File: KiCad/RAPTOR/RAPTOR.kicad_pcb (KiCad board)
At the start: 2 copper layers, 101.6 x 101.6 mm, 29 parts, among them J1 SOLC_CONN, J10 EXT_LED3, J11 SRVOL_CONN, J12 SRVOR_CONN, J14 RBF_CONN, J15 EEP_BTN_CONN, J18 CONN_BUZZER, J2 SOLP_CONN, J3 JST_2MM_MALE, J4 CONN_LED_FIX, J5 EXTENSION_HEADER, J7 EXT_LED0, J8 EXT_LED1, J9 EXT_LED2, Q1 MOSFET-NCH-STQ2NK60ZR-AP, Q2 MOSFET-NCH-STQ2NK60ZR-AP, Q3 MOSFET-NCH-STQ2NK60ZR-AP, Q4 MOSFET-NCH-STQ2NK60ZR-AP, U1 BMP280 Breakout, U2 BNO055 Breakout, U3 OpenLog, U4 AdafruitGPS, U5 Teensy3.2, U6 D24V550F5

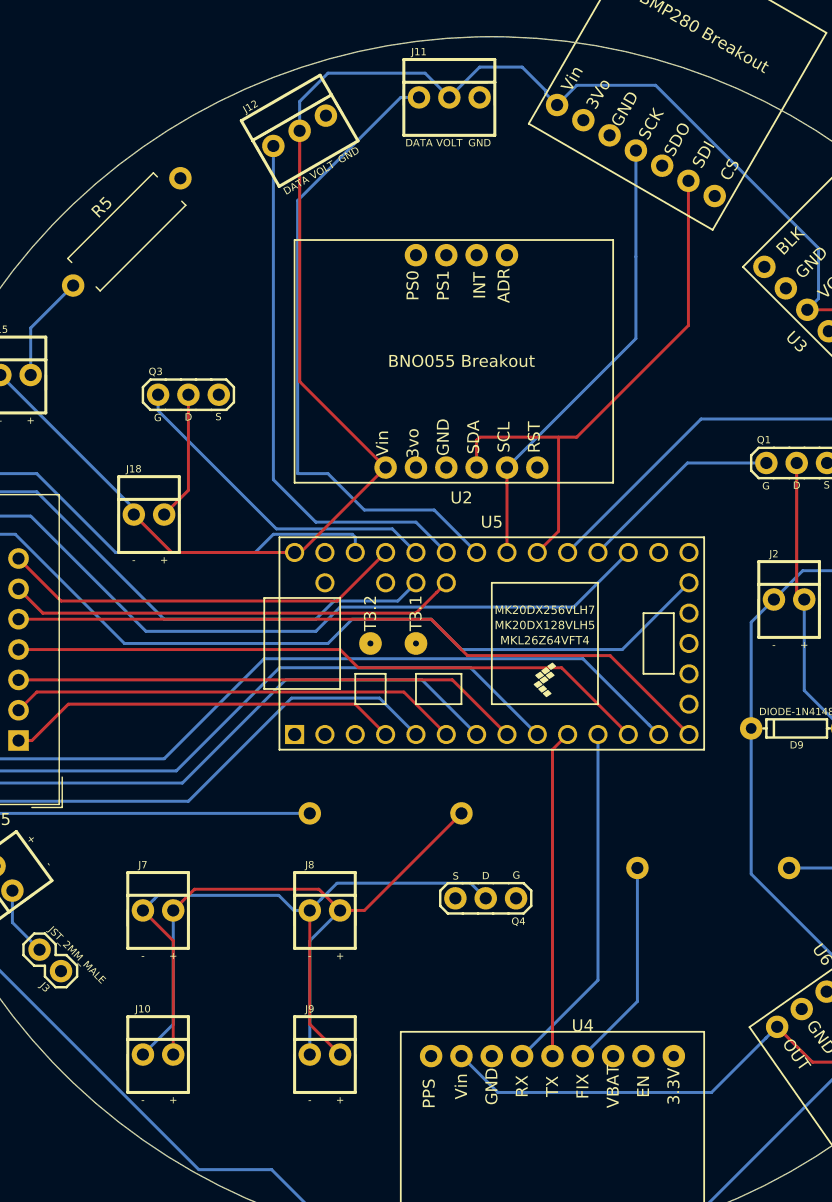
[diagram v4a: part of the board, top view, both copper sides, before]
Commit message: The Real no ground fill
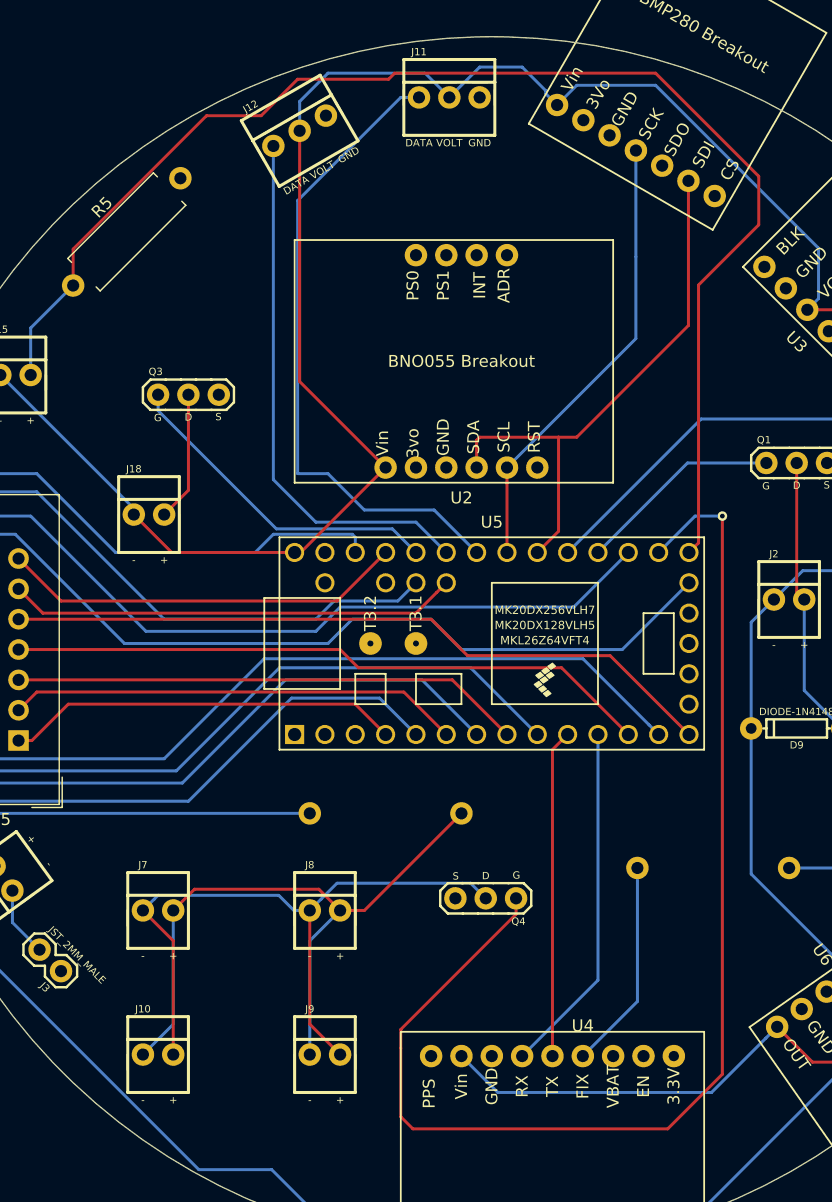
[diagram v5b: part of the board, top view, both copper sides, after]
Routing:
- net /LEDS_DTA: track 0.00 -> 104.9 mm, vias 0 -> 1
- net /EEP_BTN: track 8.97 -> 113.0 mm
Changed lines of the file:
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@@
     (thickness 1.6)
     (drawings 1)
-    (tracks 224)
+    (tracks 247)
     (zones 0)
     (modules 29)
@@
   (segment (start 101.092 62.484) (end 104.648 58.928) (width 0.25) (layer B.Cu) (net 10))
   (segment (start 101.092 66.421) (end 101.092 62.484) (width 0.25) (layer B.Cu) (net 10))
+  (segment (start 157.009999 58.890001) (end 157.009999 80.480001) (width 0.25) (layer F.Cu) (net 10))
+  (segment (start 162.052 49.784) (end 162.052 53.848) (width 0.25) (layer F.Cu) (net 10))
+  (segment (start 153.416 41.148) (end 162.052 49.784) (width 0.25) (layer F.Cu) (net 10))
+  (segment (start 162.052 53.848) (end 157.009999 58.890001) (width 0.25) (layer F.Cu) (net 10))
+  (segment (start 131.572 41.148) (end 153.416 41.148) (width 0.25) (layer F.Cu) (net 10))
+  (segment (start 157.009999 80.480001) (end 156.21 81.28) (width 0.25) (layer F.Cu) (net 10))
+  (segment (start 104.648 58.928) (end 104.648 55.88) (width 0.25) (layer F.Cu) (net 10))
+  (segment (start 104.648 55.88) (end 115.818801 44.709199) (width 0.25) (layer F.Cu) (net 10))
+  (segment (start 115.818801 44.709199) (end 120.390801 44.709199) (width 0.25) (layer F.Cu) (net 10))
+  (segment (start 120.390801 44.709199) (end 123.444 41.656) (width 0.25) (layer F.Cu) (net 10))
+  (segment (start 123.444 41.656) (end 131.064 41.656) (width 0.25) (layer F.Cu) (net 10))
+  (segment (start 131.064 41.656) (end 131.572 41.148) (width 0.25) (layer F.Cu) (net 10))
   (segment (start 114.3 76.073) (end 114.3 68.072) (width 0.25) (layer F.Cu) (net 11))
   (segment (start 112.268 78.105) (end 114.3 76.073) (width 0.25) (layer F.Cu) (net 11))
@@
   (segment (start 111.76 68.072) (end 111.76 69.401077) (width 0.25) (layer B.Cu) (net 14))
   (segment (start 131.37599 79.30599) (end 133.35 81.28) (width 0.25) (layer B.Cu) (net 14))
+  (segment (start 141.732 111.565077) (end 132.08 121.217077) (width 0.25) (layer F.Cu) (net 15))
+  (segment (start 141.732 110.236) (end 141.732 111.565077) (width 0.25) (layer F.Cu) (net 15))
+  (segment (start 132.08 121.217077) (end 132.08 122.775906) (width 0.25) (layer F.Cu) (net 15))
+  (segment (start 132.08 122.775906) (end 132.08 128.524) (width 0.25) (layer F.Cu) (net 15))
+  (segment (start 132.08 128.524) (end 133.096 129.54) (width 0.25) (layer F.Cu) (net 15))
+  (segment (start 133.096 129.54) (end 154.432 129.54) (width 0.25) (layer F.Cu) (net 15))
+  (segment (start 154.432 129.54) (end 159.004 124.968) (width 0.25) (layer F.Cu) (net 15))
+  (segment (start 159.004 124.968) (end 159.004 78.232) (width 0.25) (layer F.Cu) (net 15))
+  (via (at 159.004 78.232) (size 0.8) (drill 0.4) (layers F.Cu B.Cu) (net 15))
+  (segment (start 156.718 78.232) (end 153.67 81.28) (width 0.25) (layer B.Cu) (net 15))
+  (segment (start 159.004 78.232) (end 156.718 78.232) (width 0.25) (layer B.Cu) (net 15))
   (segment (start 91.948 103.124) (end 124.46 103.124) (width 0.25) (layer B.Cu) (net 16))
   (segment (start 91.44 76.708) (end 91.44 102.616) (width 0.25) (layer B.Cu) (net 16))
